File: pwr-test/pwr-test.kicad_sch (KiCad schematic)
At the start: 11 parts, among them J1 PINHD_1x2_Male, J2 PINHD_1x2_Male, U1 LMR54410DBVR

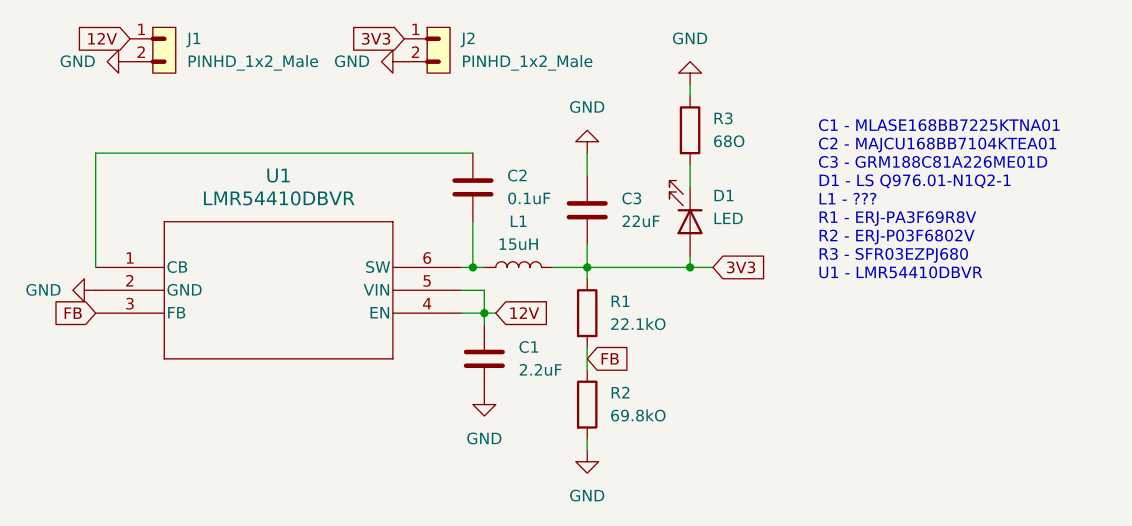
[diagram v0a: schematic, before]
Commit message: Added inductor to test pwr board
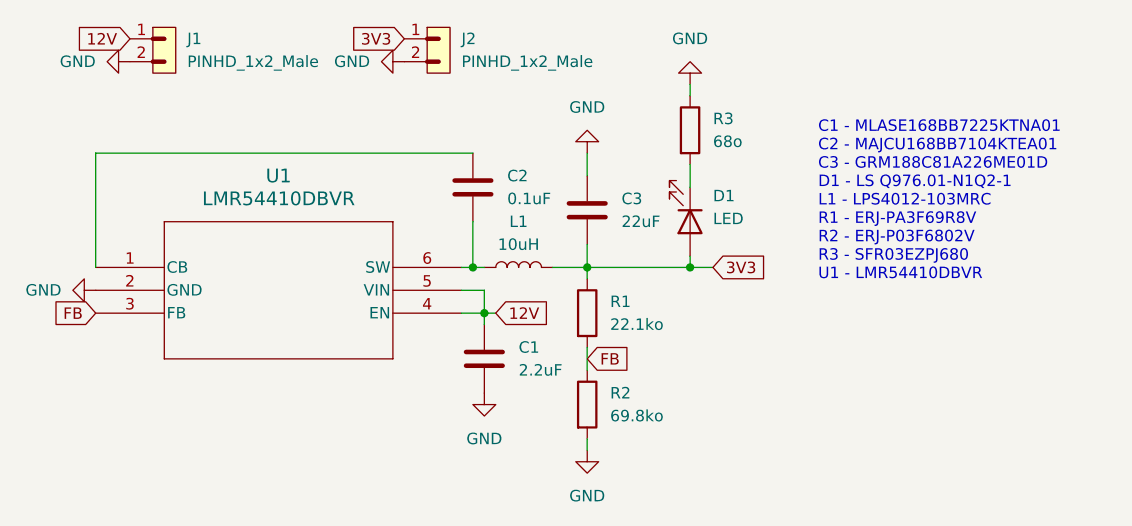
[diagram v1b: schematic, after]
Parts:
- L1: value 15uH -> 10uH
- R1: value 22.1kO -> 22.1ko
- R2: value 69.8kO -> 69.8ko
- R3: value 68O -> 68o
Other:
- note added: "C1 - MLASE168BB7225KTNA01 C2 - MAJCU168BB7104KTEA01 C3 - GRM188C81A226ME01D D1 - LS Q976.01-N1Q2-1 L1 - LPS4012-103MRC R1 - ERJ-PA3F69R8V R2 - ERJ-P03F6802V R3 - SFR03EZPJ680 U1 - LMR54410DBVR"
- note removed: "C1 - MLASE168BB7225KTNA01 C2 - MAJCU168BB7104KTEA01 C3 - GRM188C81A226ME01D D1 - LS Q976.01-N1Q2-1 L1 - ??? R1 - ERJ-PA3F69R8V R2 - ERJ-P03F6802V R3 - SFR03EZPJ680 U1 - LMR54410DBVR"
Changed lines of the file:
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@@
 	(generator_version "9.0")
 	(paper "A4")
-	(text "C1 - MLASE168BB7225KTNA01\nC2 - MAJCU168BB7104KTEA01\nC3 - GRM188C81A226ME01D\nD1 - LS Q976.01-N1Q2-1\nL1 - ???\nR1 - ERJ-PA3F69R8V\nR2 - ERJ-P03F6802V\nR3 - SFR03EZPJ680\nU1 - LMR54410DBVR"
+	(text "C1 - MLASE168BB7225KTNA01\nC2 - MAJCU168BB7104KTEA01\nC3 - GRM188C81A226ME01D\nD1 - LS Q976.01-N1Q2-1\nL1 - LPS4012-103MRC\nR1 - ERJ-PA3F69R8V\nR2 - ERJ-P03F6802V\nR3 - SFR03EZPJ680\nU1 - LMR54410DBVR"
 		(exclude_from_sim no)
 		(at 101.854 25.654 0)
@@
 			)
 		)
-		(property "Value" "68O"
+		(property "Value" "68o"
 			(at 90.17 27.9399 0)
 			(effects
@@
 			)
 		)
-		(property "Value" "22.1kO"
+		(property "Value" "22.1ko"
 			(at 78.74 48.2599 0)
 			(effects
@@
 			)
 		)
-		(property "Value" "15uH"
+		(property "Value" "10uH"
 			(at 68.58 39.37 90)
 			(effects
@@
 			)
 		)
-		(property "Value" "69.8kO"
+		(property "Value" "69.8ko"
 			(at 78.74 58.4199 0)
 			(effects
